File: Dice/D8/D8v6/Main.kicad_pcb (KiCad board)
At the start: 2 copper layers, 64.9 x 44.8 mm, 66 parts, among them J1 Conn_01x14, J2 Conn_01x04, J3 Conn_01x02, J4 DNP, P5 COILA, P6 COILB, U1 N52810_QFN32, U2 KXTJ3-1057, U3 PJ75AL50SA, U4 ME6215, U5 MCP73832T-2ACI/OT, U6 MT9700, U7 SN74LVC1G08, U8 TMR1366, Y1 32MHz 40ppm

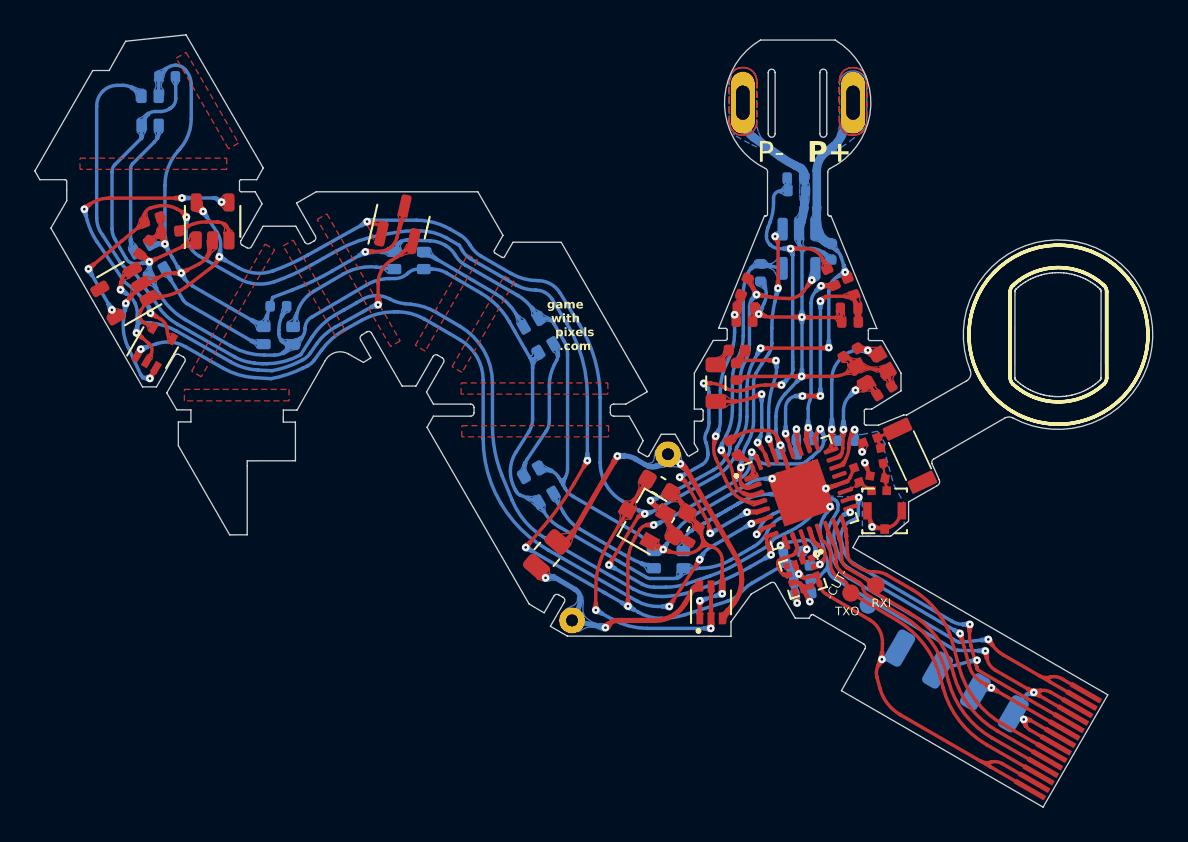
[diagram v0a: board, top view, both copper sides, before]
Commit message: Updated LCC PCB, updated dice fpc. Moved LCC testing jig
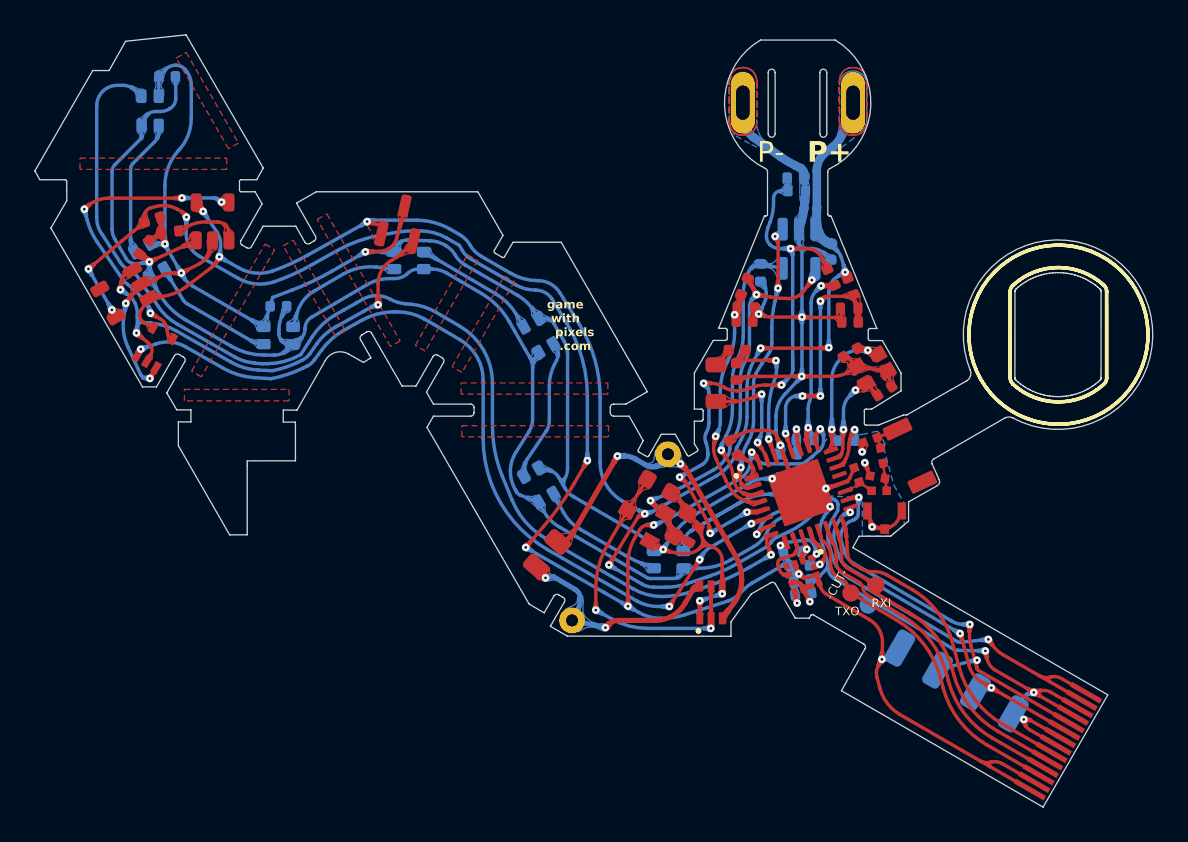
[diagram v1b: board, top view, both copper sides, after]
